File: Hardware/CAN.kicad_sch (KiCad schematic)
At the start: 19 parts, among them U4 ISOW1044

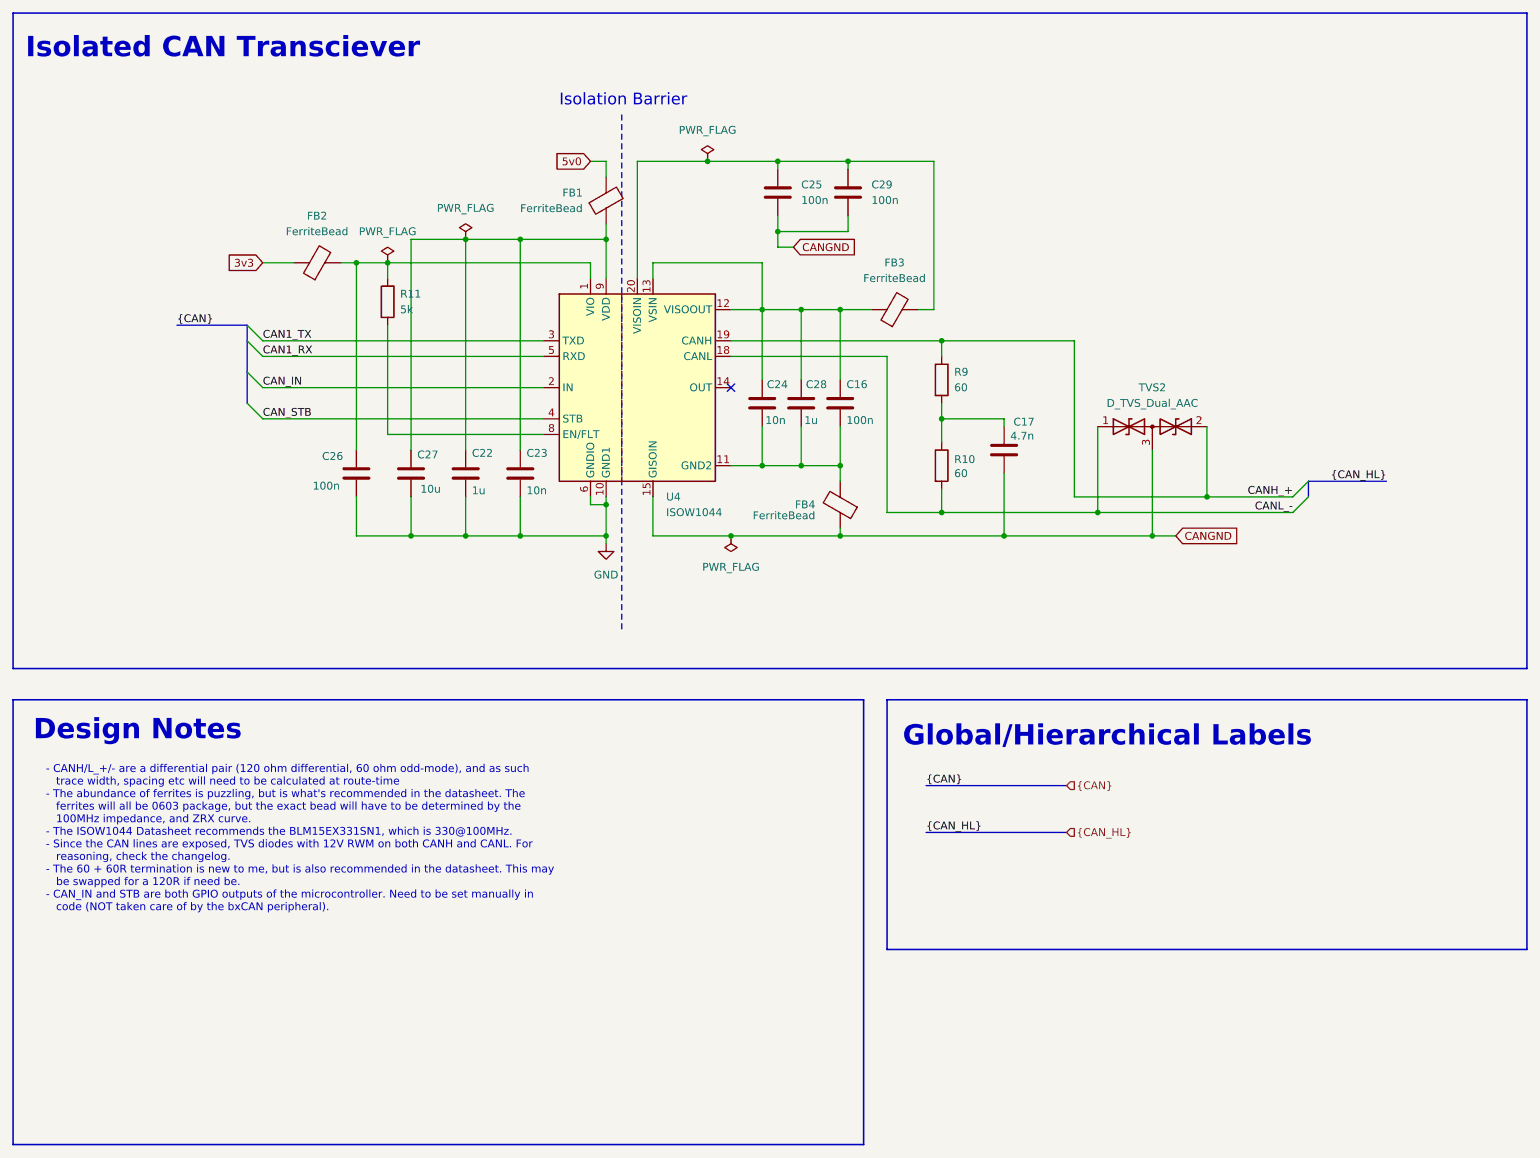
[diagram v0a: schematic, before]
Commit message: Fixed up the schematic a little, and did *most* footprint assigning
- Most footprints are assigned. Ones that arent either don't exist, or
  are out of stock at digikey and are thus not work making/adding.
- Details of next steps will be put into changelog soon
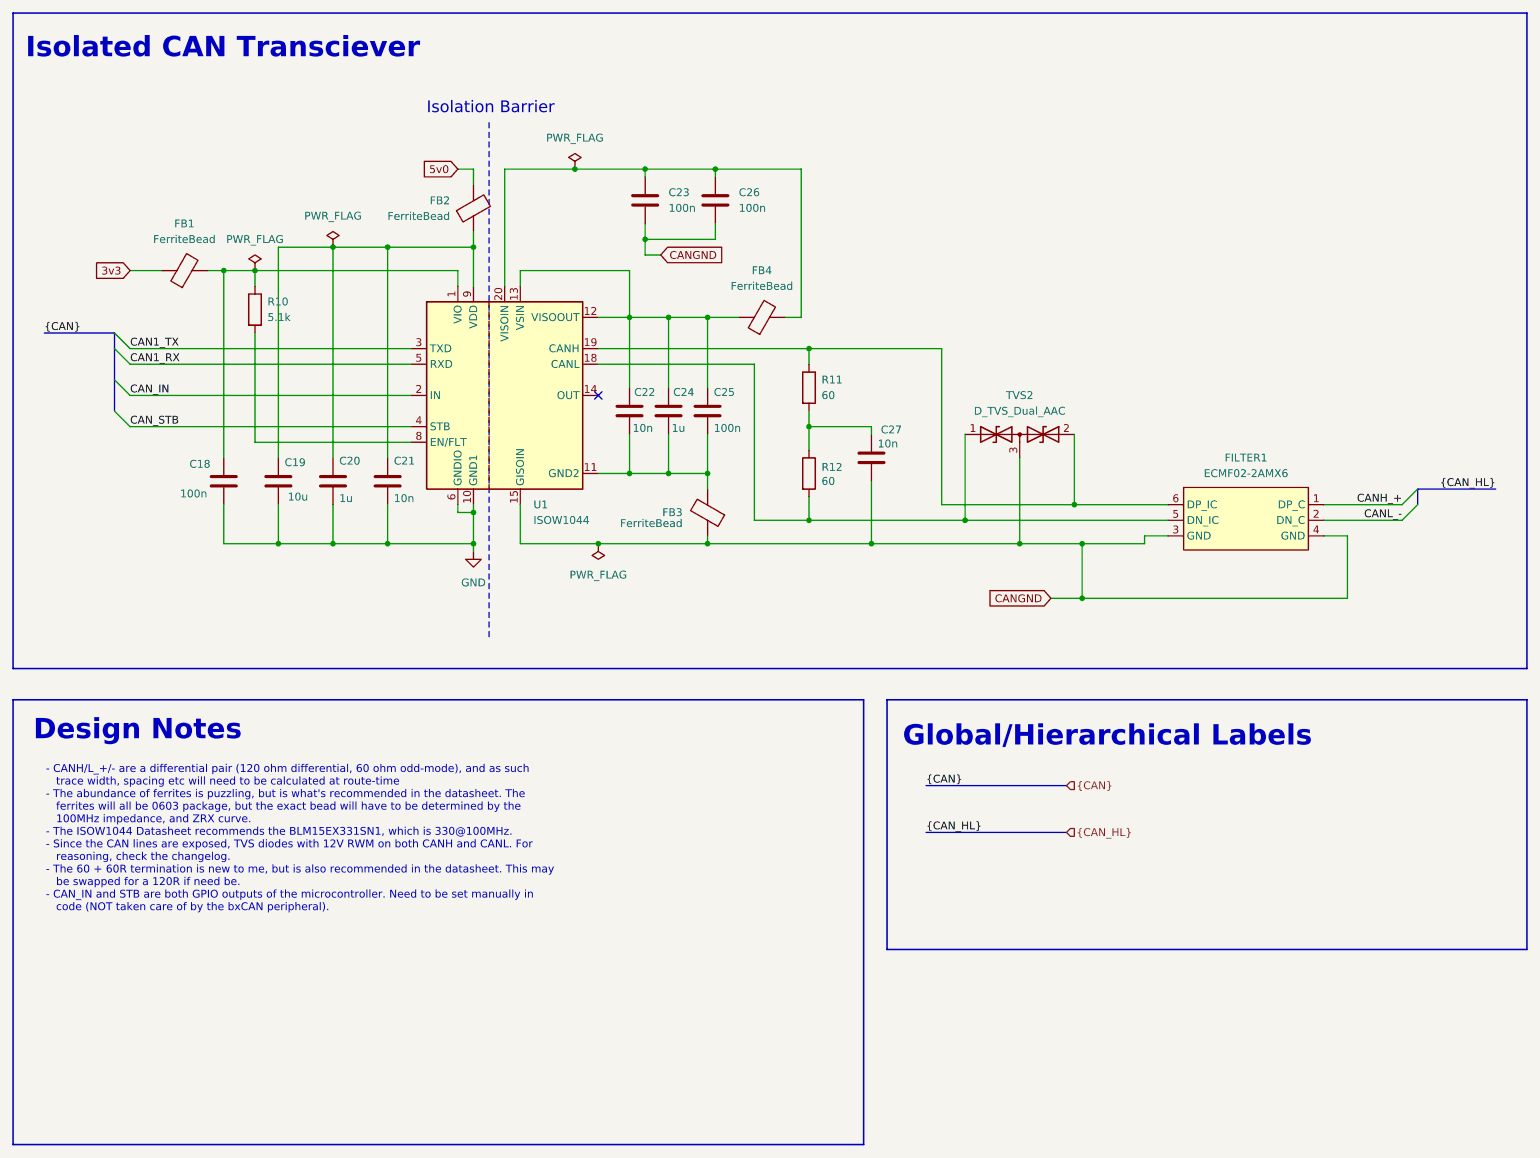
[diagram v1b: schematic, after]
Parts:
- added FILTER1: ECMF02-2AMX6, symbol symbols:ECMF2-40A100N6
- C18: renamed from C26; footprint (none) -> Capacitor_SMD:C_0603_1608Metric_Pad1.08x0.95mm_HandSolder
- C19: renamed from C27; footprint (none) -> Capacitor_SMD:C_0603_1608Metric_Pad1.08x0.95mm_HandSolder
- C20: renamed from C22; footprint (none) -> Capacitor_SMD:C_0603_1608Metric_Pad1.08x0.95mm_HandSolder
- C21: renamed from C23; footprint (none) -> Capacitor_SMD:C_0603_1608Metric_Pad1.08x0.95mm_HandSolder
- C22: renamed from C24; footprint (none) -> Capacitor_SMD:C_0603_1608Metric_Pad1.08x0.95mm_HandSolder
- C23: renamed from C25; footprint (none) -> Capacitor_SMD:C_0603_1608Metric_Pad1.08x0.95mm_HandSolder
- C24: renamed from C28; footprint (none) -> Capacitor_SMD:C_0603_1608Metric_Pad1.08x0.95mm_HandSolder
- C25: renamed from C16; footprint (none) -> Capacitor_SMD:C_0603_1608Metric_Pad1.08x0.95mm_HandSolder
- C26: renamed from C29; footprint (none) -> Capacitor_SMD:C_0603_1608Metric_Pad1.08x0.95mm_HandSolder
- C27: renamed from C17; value 4.7n -> 10n; footprint (none) -> Capacitor_SMD:C_0603_1608Metric_Pad1.08x0.95mm_HandSolder
- FB1: renamed from FB2; footprint BLM15EX331SN1D:BEADC1005X55N -> Inductor_SMD:L_0603_1608Metric_Pad1.05x0.95mm_HandSolder
- FB2: renamed from FB1; footprint BLM15EX331SN1D:BEADC1005X55N -> Inductor_SMD:L_0603_1608Metric_Pad1.05x0.95mm_HandSolder
- FB3: renamed from FB4; footprint BLM15EX331SN1D:BEADC1005X55N -> Inductor_SMD:L_0603_1608Metric_Pad1.05x0.95mm_HandSolder
- FB4: renamed from FB3; footprint BLM15EX331SN1D:BEADC1005X55N -> Inductor_SMD:L_0603_1608Metric_Pad1.05x0.95mm_HandSolder
- R10: renamed from R11; value 5k -> 5.1k; footprint (none) -> Resistor_SMD:R_0603_1608Metric_Pad0.98x0.95mm_HandSolder
- R11: renamed from R9; footprint (none) -> Resistor_SMD:R_0603_1608Metric_Pad0.98x0.95mm_HandSolder
- R12: renamed from R10; footprint (none) -> Resistor_SMD:R_0603_1608Metric_Pad0.98x0.95mm_HandSolder
- TVS2: footprint (none) -> Package_TO_SOT_SMD:SOT-23-3
- renumbered U4 to U1
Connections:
- net CANGND: now also FILTER1.3 (GND), FILTER1.4 (GND)
- net CANH_+: now also FILTER1.1 (DP_C); no longer R11.1, TVS2.2 (A2), U1.19 (CANH)
- net CANL_-: now also FILTER1.2 (DN_C); no longer R12.2, TVS2.1 (A1), U1.18 (CANL)
- new net: FILTER1.6 (DP_IC), R11.1, TVS2.2 (A2), U1.19 (CANH)
- new net: FILTER1.5 (DN_IC), R12.2, TVS2.1 (A1), U1.18 (CANL)
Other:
- moved on the sheet: C18, C19, C20, C21, C22, C23, C24, C25, C26, C27, FB1, FB2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
